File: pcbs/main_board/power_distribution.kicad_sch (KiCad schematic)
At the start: 11 parts, among them J1 BAT1, J2 BAT2, P1 USB/STEPUP, Q1 PMOS, SW1 Power switch, U5 Step-up

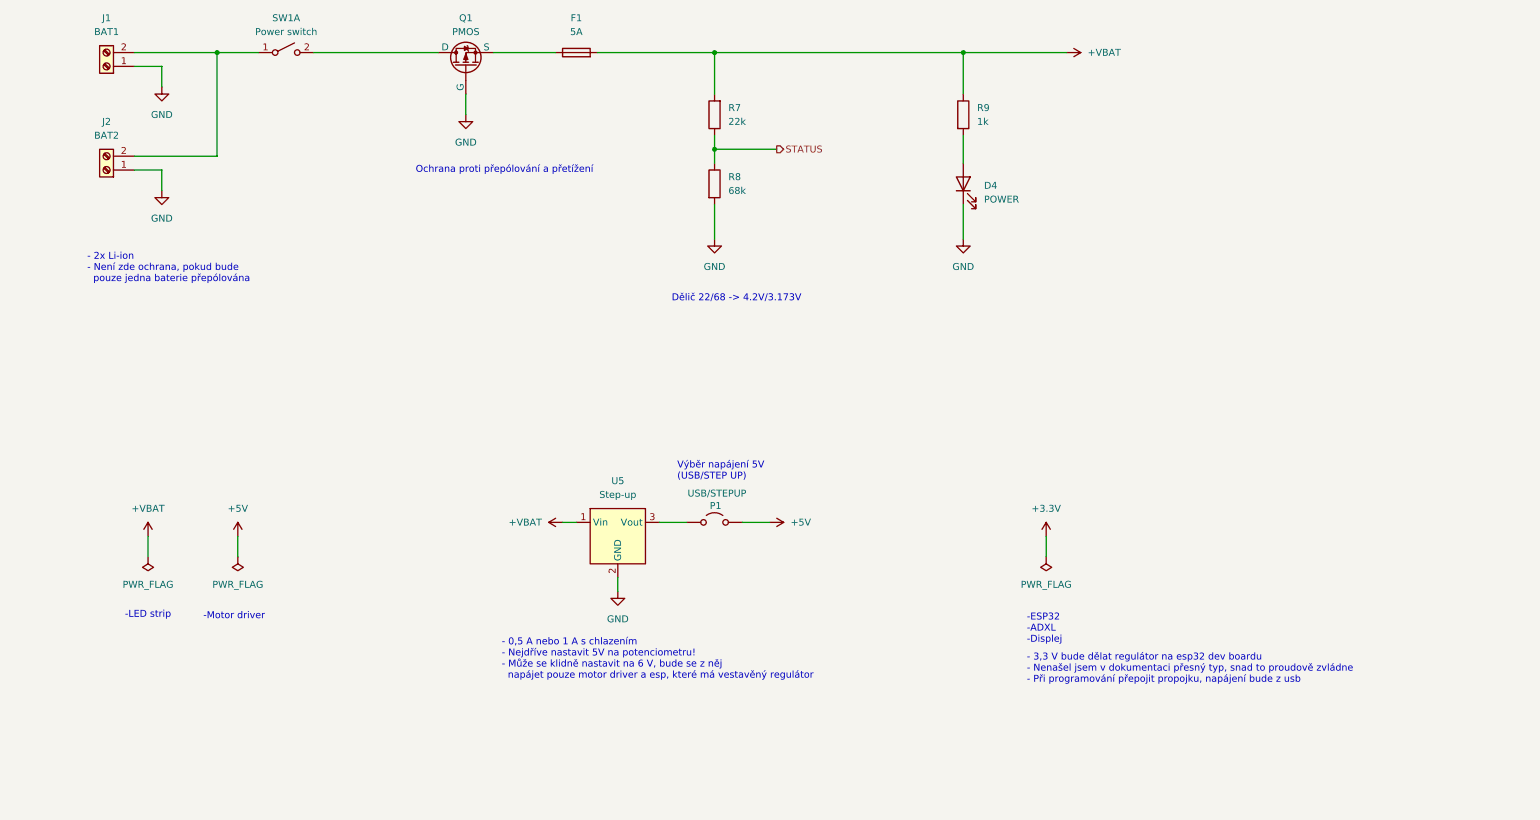
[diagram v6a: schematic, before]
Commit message: Add IC for charging
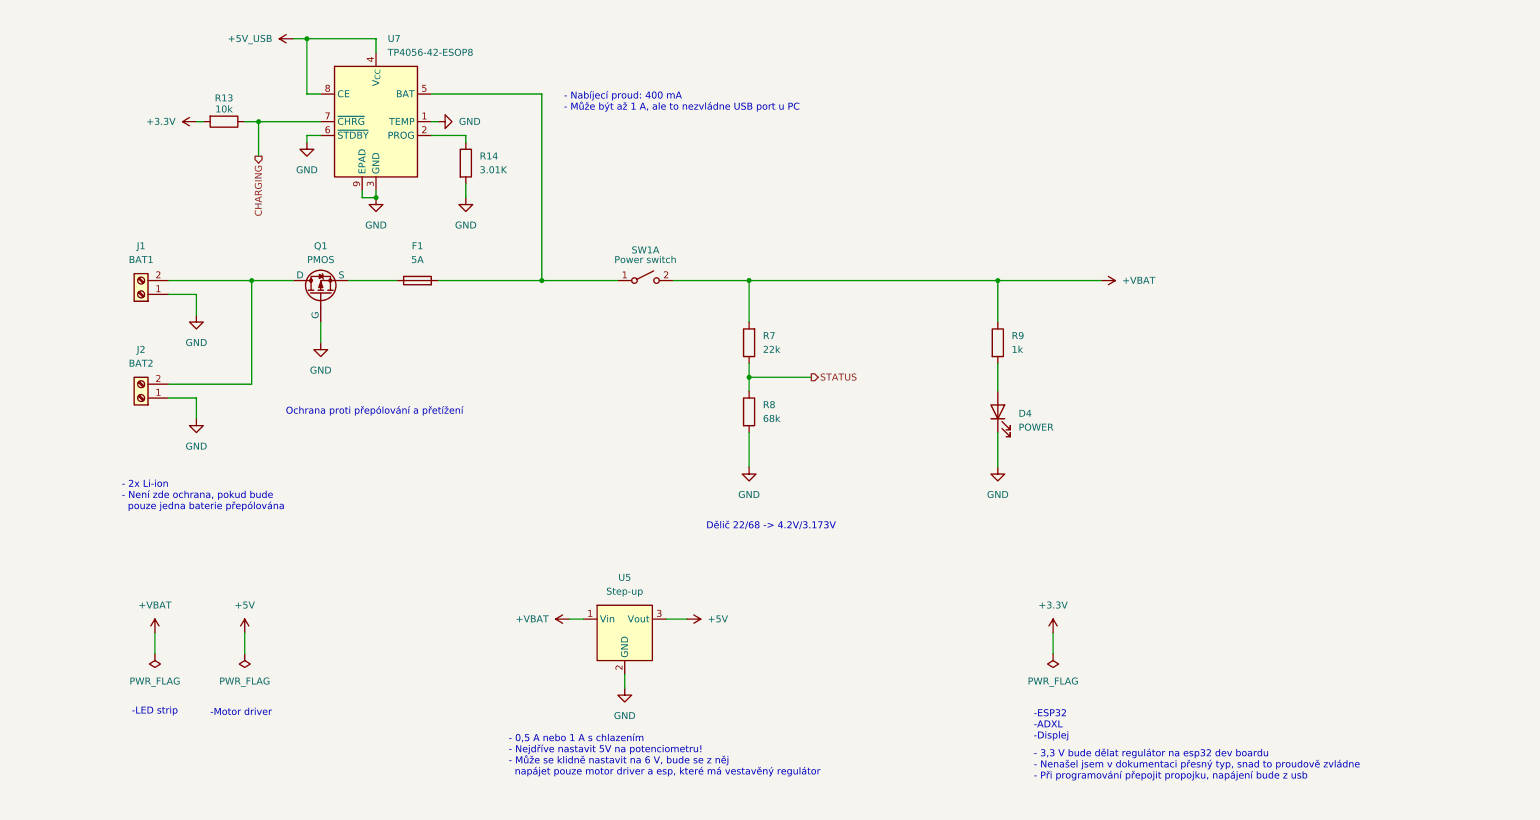
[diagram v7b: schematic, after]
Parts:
- removed P1: USB/STEPUP, Connector_PinHeader_2.54mm:PinHeader_1x03_P2.54mm_Horizontal, symbol Jumper:Jumper_2_Open
- added R13: 10k, Resistor_SMD:R_0603_1608Metric_Pad0.98x0.95mm_HandSolder, symbol Device:R
- added R14: 3.01K, Resistor_SMD:R_0603_1608Metric_Pad0.98x0.95mm_HandSolder, symbol Device:R
- added U7: TP4056-42-ESOP8, Package_SO:SOIC-8-1EP_3.9x4.9mm_P1.27mm_EP2.41x3.3mm_ThermalVias, symbol Battery_Management:TP4056-42-ESOP8
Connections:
- net +3.3V: now also R13.2
- net +5V: now also U5.3 (Vout)
- net +VBAT: now also SW1.2 (B); no longer F1.2
- net GND: now also R14.2, U7.1 (TEMP), U7.3 (GND), U7.6 (~{STDBY}), U7.9 (EPAD)
- net at Q1.1 (D): now also J1.2 (Pin_2), J2.2 (Pin_2); no longer SW1.2 (B)
- new net: R14.1, U7.2 (PROG)
- new net: F1.2, SW1.1 (A), U7.5 (BAT)
- new net +5V_USB: U7.4 (V_{CC}), U7.8 (CE)
- new net CHARGING: R13.1, U7.7 (~{CHRG})
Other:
- note added: "- Nabíjecí proud: 400 mA - Může být až 1 A, ale to nezvládne USB port u PC"
- note removed: "Výběr napájení 5V (USB/STEP UP)"
- moved on the sheet: D4, F1, J1, J2, Q1, R7, R8, R9, SW1A, U5

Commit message: Add 3V3 regulator
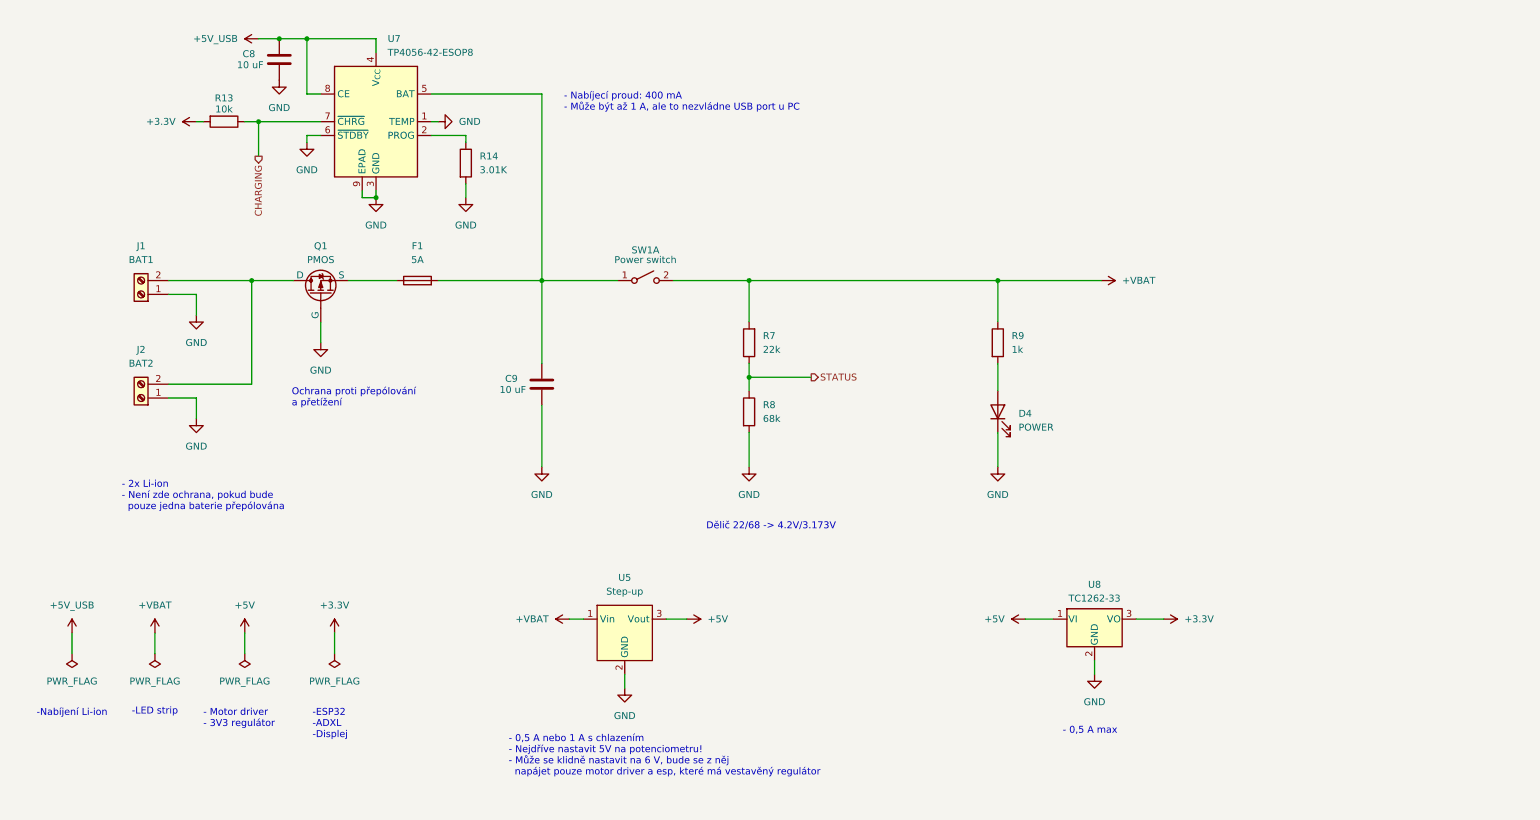
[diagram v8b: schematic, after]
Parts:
- added C8, C9: 10 uF, Capacitor_SMD:C_0603_1608Metric_Pad1.08x0.95mm_HandSolder, symbol Device:C
- added U8: TC1262-33, Package_TO_SOT_SMD:SOT-223-3_TabPin2, symbol Regulator_Linear:TC1262-33
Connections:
- net +3.3V: now also U8.3 (VO)
- net +5V: now also U8.1 (VI)
- net +5V_USB: now also C8.2
- net GND: now also C8.1, C9.1, U8.2 (GND)
- net at F1.2, SW1.1 (A), U7.5 (BAT): now also C9.2
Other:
- note added: "- 0,5 A max"
- note added: "- Motor driver - 3V3 regulátor"
- note added: "-Nabíjení Li-ion"
- note removed: "- 3,3 V bude dělat regulátor na esp32 dev boardu - Nenašel jsem v dokumentaci přesný typ, snad to proudově zvládne - Při programování přepojit propojku, napájení bude z usb"
- note removed: "-Motor driver"
